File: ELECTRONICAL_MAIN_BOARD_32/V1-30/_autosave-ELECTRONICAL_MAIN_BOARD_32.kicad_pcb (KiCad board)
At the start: 2 copper layers, 233.9 x 101 mm, 232 parts, among them J1 SIL1, J2 SIL1, J3 SIL1, J4 SIL1, J5 RJ12, J6 SIL1, J7 SIL1, K1 CONN_3, K2 CONN_3, K3 CONN_3, K4 CONN_3, K5 CONN_3, K6 CONN_3, K7 CONN_3, P1 HE10-16, P10 CONN_2, P11 CONN_2, P14 CAVALIER, P15 CAVALIER, P2 CONN_4, P3 CONN_4, P4 CONN_4, P5 CONN_4, P6 CONN_4, P7 CONN_4, P8 CONN_2, P9 CONN_5, Q1 BSS123, Q2 BSS123, Q3 BSS123, Q4 BSS123, SW1 SWITCH_X_8, SW2 SW_PUSH_SMALL, SW3 SWITCH_X_8, U1 PIC32MX795F512H, U2 74LVCC3245, U3 74LVCC3245, U4 PCA9306, U5 PCA9306, U6 74LVCC3245, U7 24C512, U8 LM75A, U9 PCF8563, X1 CRYSTAL1

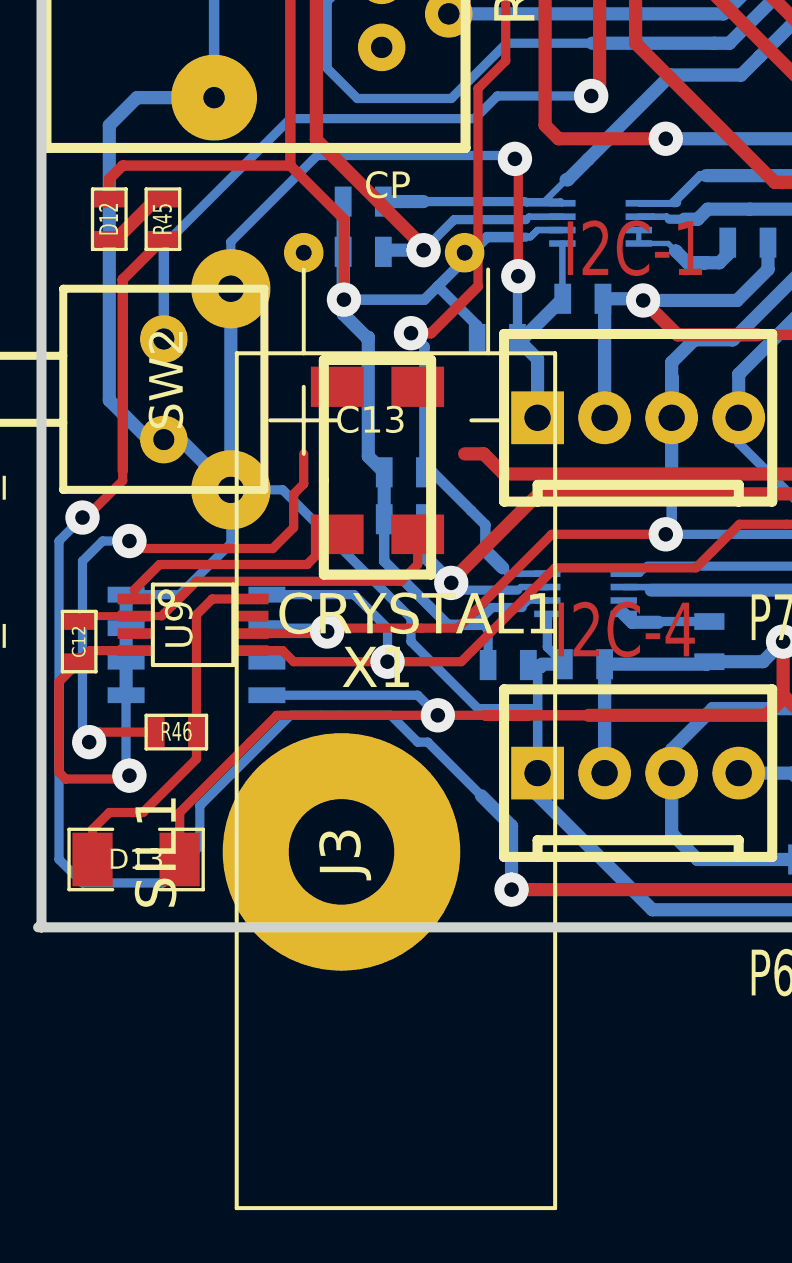
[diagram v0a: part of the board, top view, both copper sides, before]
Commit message: MAJ USB TO 4UART + ADD NEW MECHANICAL BOARD
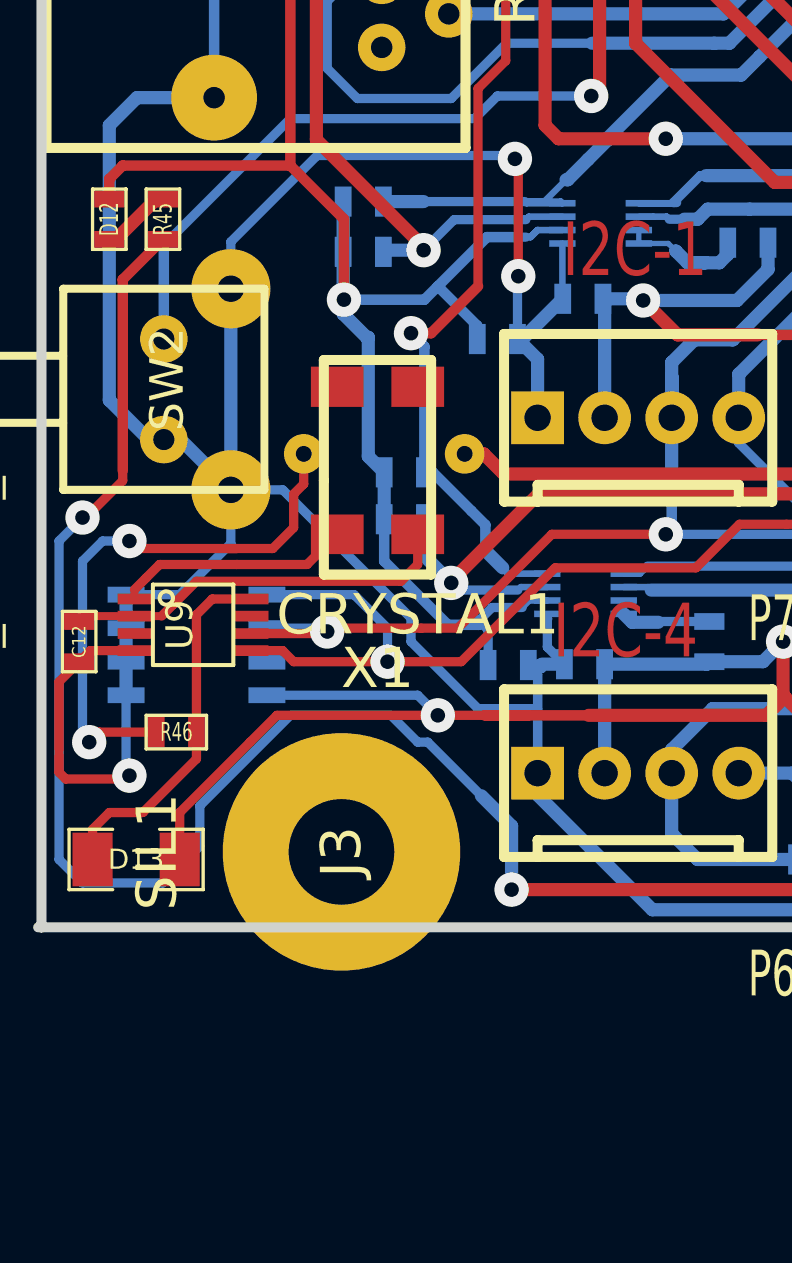
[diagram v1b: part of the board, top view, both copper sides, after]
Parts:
- C13: moved to B.Cu
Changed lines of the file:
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@@
     (pad_to_mask_clearance 0.254)
     (aux_axis_origin 0 0)
-    (visible_elements FFFFFBBF)
+    (visible_elements FFFFF9BF)
     (pcbplotparams
       (layerselection 3178497)
@@
     )
   )
-  (module C-10F (layer Dessus)
+  (module C-10F (layer Dessous)
     (at 44.45 129.54)
-    (fp_text reference C13 (at 5.08 2.54) (layer F.SilkS)
-      (effects (font (size 1 1) (thickness 0.15)))
+    (fp_text reference C13 (at 5.08 -2.54) (layer B.SilkS)
+      (effects (font (size 1 1) (thickness 0.15)) (justify mirror))
     )
-    (fp_text value CP (at 5.715 -6.35) (layer F.SilkS)
-      (effects (font (size 1 1) (thickness 0.15)))
+    (fp_text value CP (at 5.715 6.35) (layer B.SilkS)
+      (effects (font (size 1 1) (thickness 0.15)) (justify mirror))
     )
-    (fp_line (start 8.89 2.54) (end 10.16 2.54) (layer F.SilkS) (width 0.15))
-    (fp_line (start 1.27 2.54) (end 3.81 2.54) (layer F.SilkS) (width 0.15))
-    (fp_line (start 2.54 1.27) (end 2.54 3.81) (layer F.SilkS) (width 0.15))
-    (fp_line (start 2.54 -3.175) (end 2.54 0) (layer F.SilkS) (width 0.15))
-    (fp_line (start 9.525 -3.175) (end 9.525 0) (layer F.SilkS) (width 0.15))
-    (fp_line (start 12.065 0) (end 12.065 32.385) (layer F.SilkS) (width 0.15))
-    (fp_line (start 12.065 32.385) (end 0 32.385) (layer F.SilkS) (width 0.15))
-    (fp_line (start 0 0) (end 0 32.385) (layer F.SilkS) (width 0.15))
-    (fp_line (start 0 0) (end 12.065 0) (layer F.SilkS) (width 0.15))
-    (pad 1 thru_hole circle (at 2.54 -3.81) (size 1.5 1.5) (drill 0.6)
-      (layers *.Cu *.Mask F.SilkS)
+    (fp_line (start 8.89 -2.54) (end 10.16 -2.54) (layer B.SilkS) (width 0.15))
+    (fp_line (start 1.27 -2.54) (end 3.81 -2.54) (layer B.SilkS) (width 0.15))
+    (fp_line (start 2.54 -1.27) (end 2.54 -3.81) (layer B.SilkS) (width 0.15))
+    (fp_line (start 2.54 3.175) (end 2.54 0) (layer B.SilkS) (width 0.15))
+    (fp_line (start 9.525 3.175) (end 9.525 0) (layer B.SilkS) (width 0.15))
+    (fp_line (start 12.065 0) (end 12.065 -32.385) (layer B.SilkS) (width 0.15))
+    (fp_line (start 12.065 -32.385) (end 0 -32.385) (layer B.SilkS) (width 0.15))
+    (fp_line (start 0 0) (end 0 -32.385) (layer B.SilkS) (width 0.15))
+    (fp_line (start 0 0) (end 12.065 0) (layer B.SilkS) (width 0.15))
+    (pad 1 thru_hole circle (at 2.54 3.81) (size 1.5 1.5) (drill 0.6)
+      (layers *.Cu *.Mask B.SilkS)
       (net 93 N-00000115)
     )
-    (pad 2 thru_hole circle (at 8.636 -3.81) (size 1.5 1.5) (drill 0.6)
-      (layers *.Cu *.Mask F.SilkS)
+    (pad 2 thru_hole circle (at 8.636 3.81) (size 1.5 1.5) (drill 0.6)
+      (layers *.Cu *.Mask B.SilkS)
       (net 89 N-00000111)
     )
